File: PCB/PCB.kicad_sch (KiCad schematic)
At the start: 0 parts

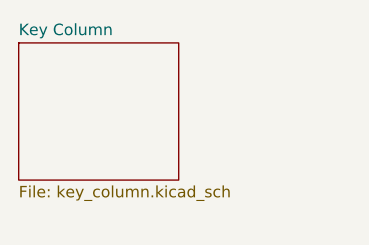
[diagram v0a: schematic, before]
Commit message: Figured out the layout, now working on the PCB for each half.
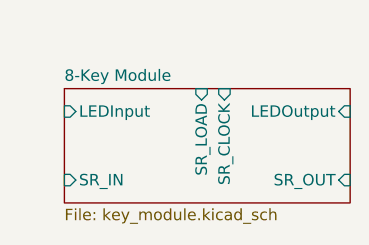
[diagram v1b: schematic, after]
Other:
- removed sheet Key Column
- added sheet 8-Key Module (key_module.kicad_sch)
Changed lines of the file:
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@@
 (kicad_sch (version 20230121) (generator eeschema)
   (paper "A4")
-  (sheet (at 33.02 27.94) (size 17.78 15.24) (fields_autoplaced)
+  (sheet (at 38.1 33.02) (size 31.75 12.7) (fields_autoplaced)
     (stroke (width 0.1524) (type solid))
     (fill (color 0 0 0 0.0000))
-    (property "Sheetname" "Key Column" (at 33.02 27.2284 0)
+    (property "Sheetname" "8-Key Module" (at 38.1 32.3084 0)
       (effects (font (size 1.27 1.27)) (justify left bottom))
     )
-    (property "Sheetfile" "key_column.kicad_sch" (at 33.02 43.7646 0)
+    (property "Sheetfile" "key_module.kicad_sch" (at 38.1 46.3046 0)
       (effects (font (size 1.27 1.27)) (justify left top))
+    )
+    (pin "LEDInput" input (at 38.1 35.56 180)
+      (effects (font (size 1.27 1.27)) (justify left))
+    )
+    (pin "SR_OUT" input (at 69.85 43.18 0)
+      (effects (font (size 1.27 1.27)) (justify right))
+    )
+    (pin "SR_IN" input (at 38.1 43.18 180)
+      (effects (font (size 1.27 1.27)) (justify left))
+    )
+    (pin "SR_LOAD" input (at 53.34 33.02 90)
+      (effects (font (size 1.27 1.27)) (justify right))
+    )
+    (pin "SR_CLOCK" input (at 55.88 33.02 90)
+      (effects (font (size 1.27 1.27)) (justify right))
+    )
+    (pin "LEDOutput" input (at 69.85 35.56 0)
+      (effects (font (size 1.27 1.27)) (justify right))
     )
     (instances
       (project "PCB"
-        (path "/d2f5552d-48c0-49b0-8e54-6764f47ed1da" (page "2"))
+        (path "/d2f5552d-48c0-49b0-8e54-6764f47ed1da" (page "11"))
       )
     )

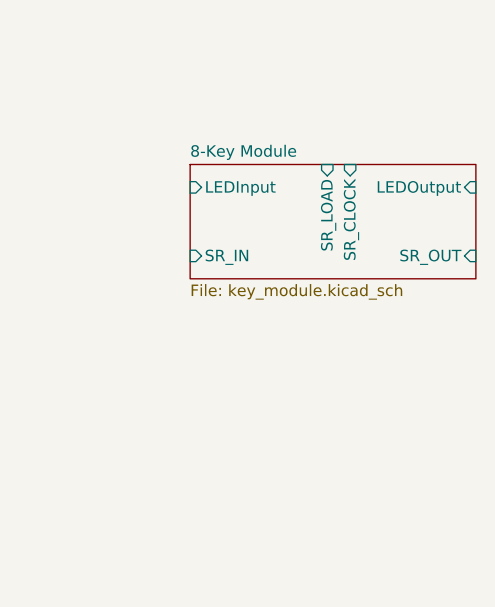
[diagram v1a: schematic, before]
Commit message: Working on STM32 circuit
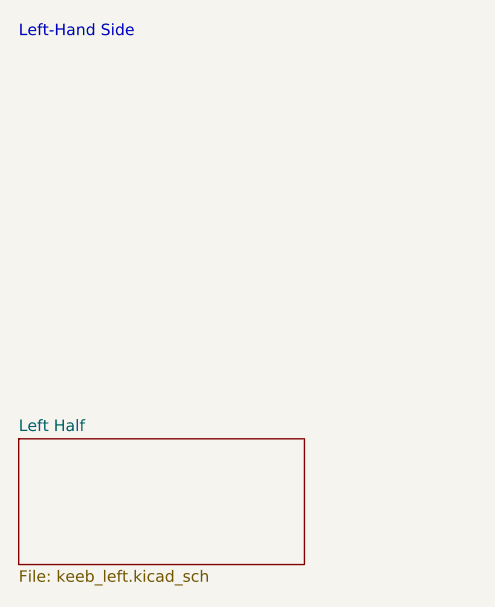
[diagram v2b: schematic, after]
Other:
- removed sheet 8-Key Module
- added sheet Left Half (keeb_left.kicad_sch)
- note added: "Left-Hand Side"
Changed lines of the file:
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@@
 (kicad_sch (version 20230121) (generator eeschema)
   (paper "A4")
-  (sheet (at 38.1 33.02) (size 31.75 12.7) (fields_autoplaced)
+  (text "Left-Hand Side" (at 19.05 19.05 0)
+    (effects (font (size 1.27 1.27)) (justify left bottom))
+  )
+  (sheet (at 19.05 63.5) (size 31.75 13.97) (fields_autoplaced)
     (stroke (width 0.1524) (type solid))
     (fill (color 0 0 0 0.0000))
-    (property "Sheetname" "8-Key Module" (at 38.1 32.3084 0)
+    (property "Sheetname" "Left Half" (at 19.05 62.7884 0)
       (effects (font (size 1.27 1.27)) (justify left bottom))
     )
-    (property "Sheetfile" "key_module.kicad_sch" (at 38.1 46.3046 0)
+    (property "Sheetfile" "keeb_left.kicad_sch" (at 19.05 78.0546 0)
       (effects (font (size 1.27 1.27)) (justify left top))
-    )
-    (pin "LEDInput" input (at 38.1 35.56 180)
-      (effects (font (size 1.27 1.27)) (justify left))
-    )
-    (pin "SR_OUT" input (at 69.85 43.18 0)
-      (effects (font (size 1.27 1.27)) (justify right))
-    )
-    (pin "SR_IN" input (at 38.1 43.18 180)
-      (effects (font (size 1.27 1.27)) (justify left))
-    )
-    (pin "SR_LOAD" input (at 53.34 33.02 90)
-      (effects (font (size 1.27 1.27)) (justify right))
-    )
-    (pin "SR_CLOCK" input (at 55.88 33.02 90)
-      (effects (font (size 1.27 1.27)) (justify right))
-    )
-    (pin "LEDOutput" input (at 69.85 35.56 0)
-      (effects (font (size 1.27 1.27)) (justify right))
     )
     (instances
       (project "PCB"
-        (path "/d2f5552d-48c0-49b0-8e54-6764f47ed1da" (page "11"))
+        (path "/d2f5552d-48c0-49b0-8e54-6764f47ed1da" (page "113"))
       )
     )
